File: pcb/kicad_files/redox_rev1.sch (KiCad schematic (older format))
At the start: 76 parts, among them K0 KEYSW, K1 KEYSW, K10 KEYSW, K11 KEYSW, K12 KEYSW, K13 KEYSW, K14 KEYSW, K15 KEYSW, K16 KEYSW, K2 KEYSW, K20 KEYSW, K21 KEYSW, K22 KEYSW, K23 KEYSW, K24 KEYSW, K25 KEYSW, K26 KEYSW, K3 KEYSW, K30 KEYSW, K31 KEYSW, K32 KEYSW, K33 KEYSW, K34 KEYSW, K35 KEYSW, K36 KEYSW, K4 KEYSW, K40 KEYSW, K41 KEYSW, K42 KEYSW, K43 KEYSW, K44 KEYSW, K45 KEYSW, K46 KEYSW, K5 KEYSW, K6 KEYSW, U1 ProMicro

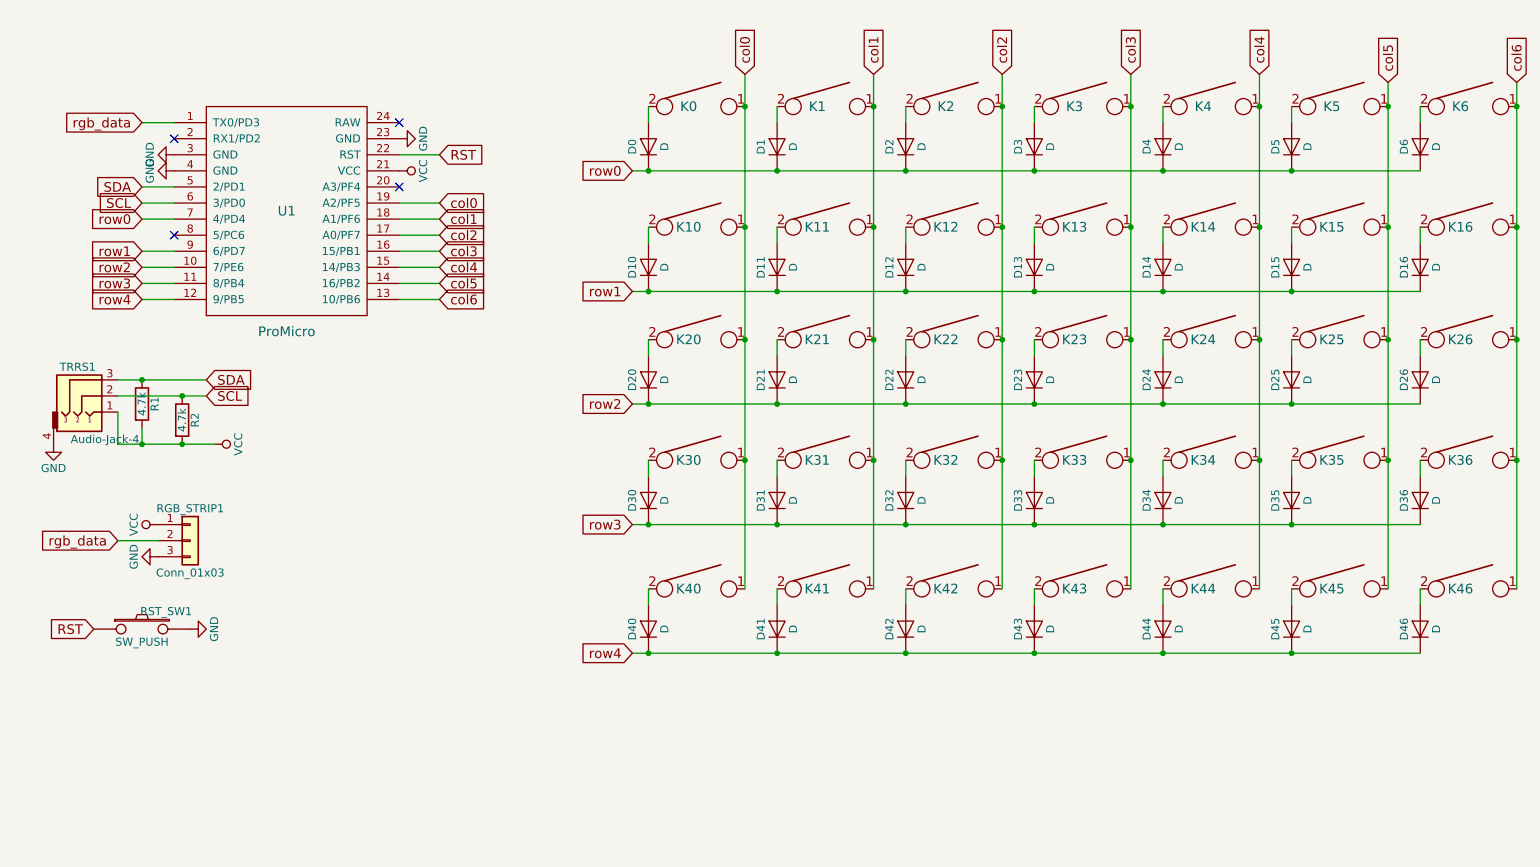
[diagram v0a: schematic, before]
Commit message: included oled updates
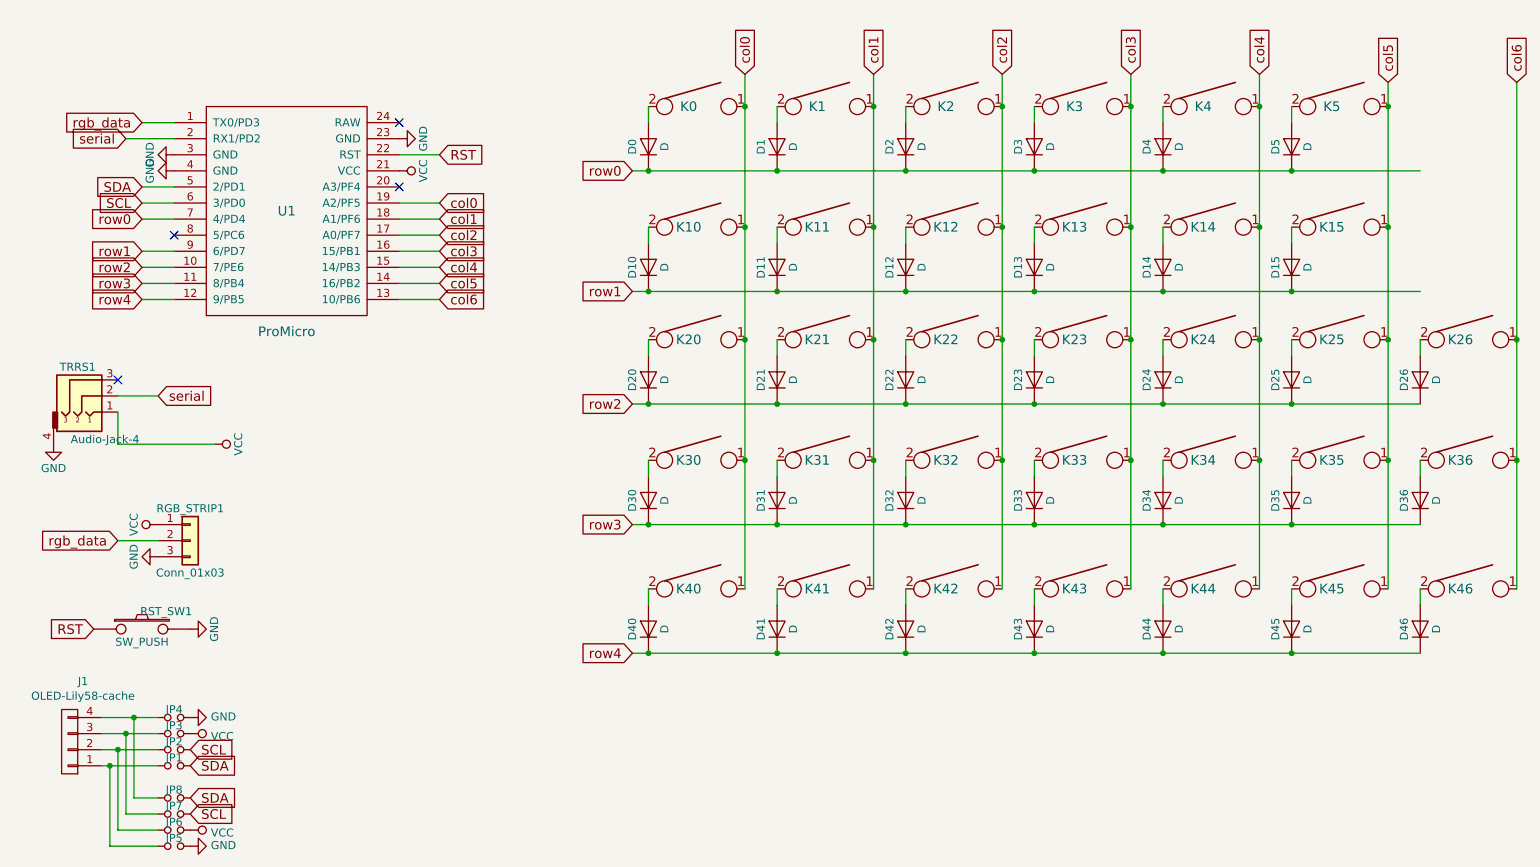
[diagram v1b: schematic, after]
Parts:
- removed D16, D6: D, Keebio-Parts:Diode-dual, symbol Device:D
- removed K16, K6: KEYSW, keyswitches:SW_MX_reversible, symbol redox_rev1-rescue:KEYSW
- removed R1, R2: 4.7k, Keebio-Parts:Resistor-Compact, symbol Device:R
- added J1: OLED-Lily58-cache, Lily58_Pro-footprint:OLED_4Pin, symbol Lily58_Pro-rescue:OLED-Lily58-cache
- added JP1, JP2, JP3, JP4, JP5, JP6, JP7, JP8: Jumper_NO_Small, Lily58_Pro-footprint:Jumper, symbol Device:Jumper_NO_Small
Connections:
- net GND: now also JP4.2, JP5.2
- net SCL: now also JP2.2, JP7.2; no longer TRRS1.2
- net SDA: now also JP1.2, JP8.2; no longer TRRS1.3
- net VCC: now also JP3.2, JP6.2
- net serial: now reaches U1.2 (RX1/PD2)
- net serial: now also TRRS1.2
- new net: J1.1 (P1), JP1.1, JP5.1
- new net: J1.2 (P2), JP2.1, JP6.1
- new net: J1.3 (P3), JP3.1, JP7.1
- new net: J1.4 (P4), JP4.1, JP8.1
